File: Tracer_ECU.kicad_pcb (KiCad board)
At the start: 4 copper layers, 82 x 54.8 mm, 148 parts, among them IC1 R5F566TEADFM#30, IC2 MPU-6500, IC3 DRV8300DPWR, IC4 DRV8300DPWR, J1 BAT, J10 ENC2, J11 ENC2_SPI, J12 LCD, J13 SDC, J14 FAN, J15 ENC1_SPI, J2 DBG, J3 TSL1401, J4 MSENS1, J5 MOT1, J6 LIGHIT, J7 MSENS2, J8 MOT2, J9 ENC1, Q1 TJ8S06M3L(T6L1,NQ), Q2 FDS6898A, Q3 FDS6898A, Q4 FDS6898A, Q5 IRLML6344TRPBF, Q6 IRLML6344TRPBF, Q7 FDS6898A, Q8 FDS6898A, Q9 FDS6898A, SW1 SW_SPDT, SW2 SW_Push, SW4 SW_Push, SW5 SW_Push, U1 NJM2732, U2 AZ1117-3.3, Y1 CSTNE20M

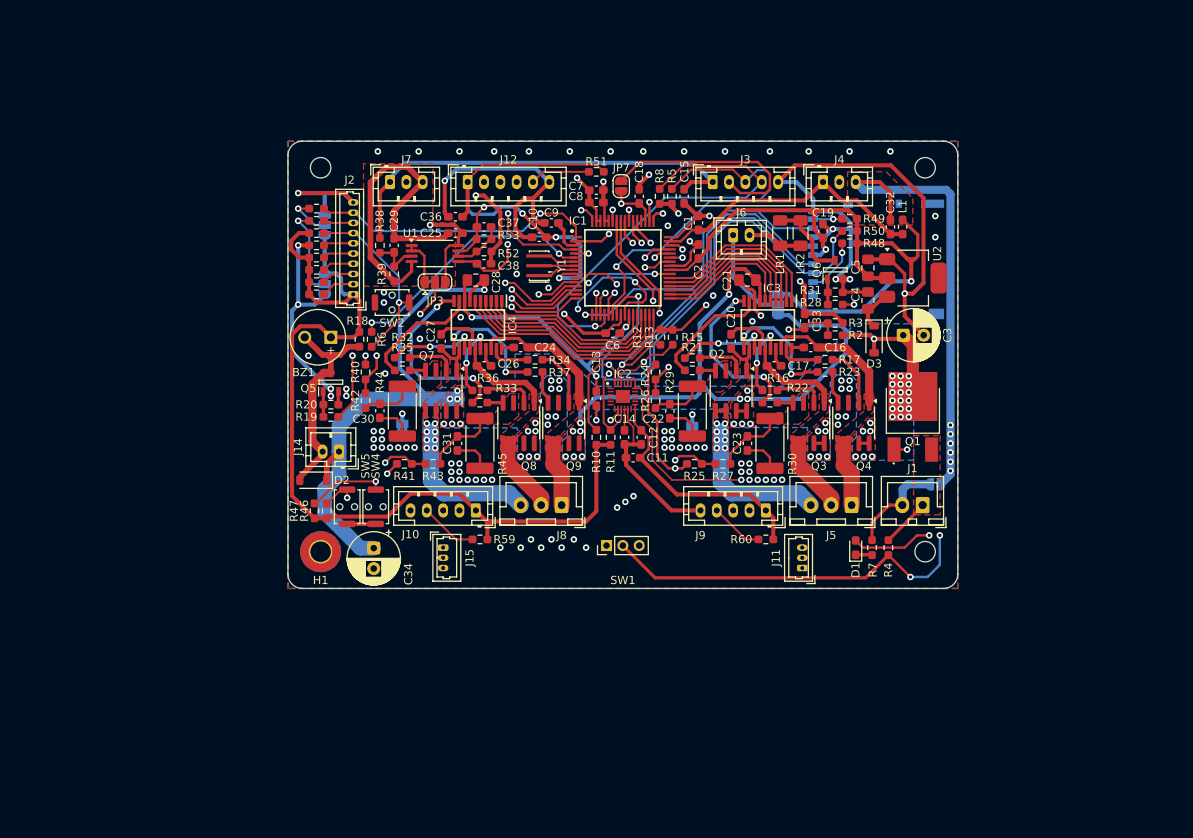
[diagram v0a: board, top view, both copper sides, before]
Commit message: ゲートドライバを変更
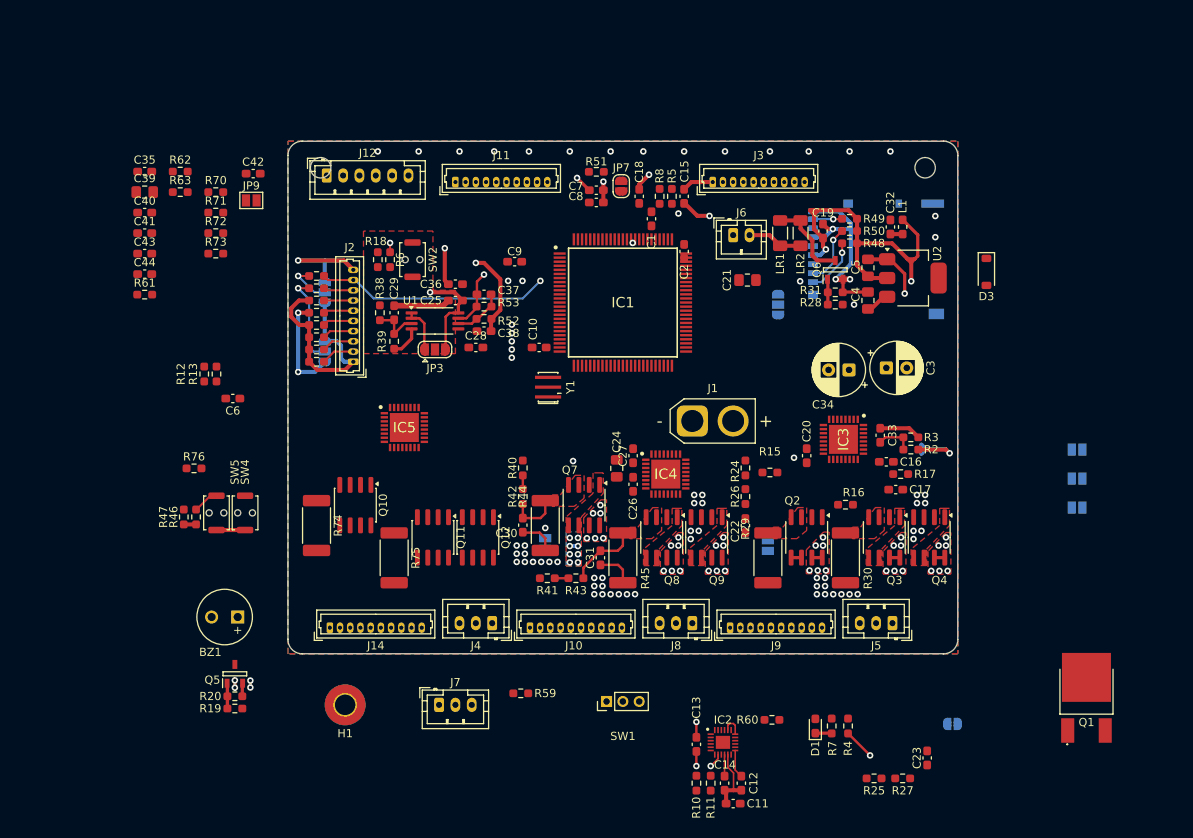
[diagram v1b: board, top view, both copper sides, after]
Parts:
- removed D2: D, Diode_SMD:D_SOD-123
- removed J15: ENC1_SPI, Connector_Molex:Molex_PicoBlade_53047-0310_1x03_P1.25mm_Vertical
- removed R21, R22, R23, R32, R33, R34, R35, R36, R37: 10, Resistor_SMD:R_0603_1608Metric_Pad0.98x0.95mm_HandSolder
- added C35: 0.1u, Capacitor_SMD:C_0603_1608Metric_Pad1.08x0.95mm_HandSolder, F.Cu at (71.0, 68.5)
- added C39: 22u, Capacitor_SMD:C_0805_2012Metric_Pad1.18x1.45mm_HandSolder, F.Cu at (71.0, 71.0)
- added C40: 0.1u, Capacitor_SMD:C_0603_1608Metric_Pad1.08x0.95mm_HandSolder, F.Cu at (71.0, 73.5)
- added C41: 1u, Capacitor_SMD:C_0603_1608Metric_Pad1.08x0.95mm_HandSolder, F.Cu at (71.0, 76.0)
- added C42: 47n, Capacitor_SMD:C_0603_1608Metric_Pad1.08x0.95mm_HandSolder, F.Cu at (84.2, 68.7)
- added C43: 1000p, Capacitor_SMD:C_0603_1608Metric_Pad1.08x0.95mm_HandSolder, F.Cu at (71.0, 78.5)
- added C44: 1000p, Capacitor_SMD:C_0603_1608Metric_Pad1.08x0.95mm_HandSolder, F.Cu at (71.0, 81.0)
- added IC5: DRV8320HRTVR, SamacSys_Parts:QFN50P500X500X80-33N-D, F.Cu at (102.8, 99.8)
- added JP10: JP_or_R, Jumper:SolderJumper-2_P1.3mm_Open_Pad1.0x1.5mm, B.Cu at (185.1, 109.6)
- added JP11: JP_or_R, Jumper:SolderJumper-2_P1.3mm_Open_Pad1.0x1.5mm, B.Cu at (185.1, 106.0)
- added JP12: JP_or_R, Jumper:SolderJumper-2_P1.3mm_Open_Pad1.0x1.5mm, B.Cu at (185.1, 102.5)
- added JP9: JP_or_R, Jumper:SolderJumper-2_P1.3mm_Open_Pad1.0x1.5mm, F.Cu at (84.0, 72.0)
- added Q10: FDS6898A, Package_SO:SOIC-8_3.9x4.9mm_P1.27mm, F.Cu at (96.8, 109.3)
- added Q11: FDS6898A, Package_SO:SOIC-8_3.9x4.9mm_P1.27mm, F.Cu at (106.2, 113.2)
- added Q12: FDS6898A, Package_SO:SOIC-8_3.9x4.9mm_P1.27mm, F.Cu at (111.8, 113.2)
- added R61: 4.7k, Resistor_SMD:R_0603_1608Metric_Pad0.98x0.95mm_HandSolder, F.Cu at (71.0, 83.5)
- added R62: 4.7k, Resistor_SMD:R_0603_1608Metric_Pad0.98x0.95mm_HandSolder, F.Cu at (75.3, 68.5)
- added R63: 4.7k, Resistor_SMD:R_0603_1608Metric_Pad0.98x0.95mm_HandSolder, F.Cu at (75.3, 71.0)
- added R70: 470, Resistor_SMD:R_0603_1608Metric_Pad0.98x0.95mm_HandSolder, F.Cu at (79.7, 71.0)
- added R71: 470, Resistor_SMD:R_0603_1608Metric_Pad0.98x0.95mm_HandSolder, F.Cu at (79.7, 73.5)
- added R72: 470, Resistor_SMD:R_0603_1608Metric_Pad0.98x0.95mm_HandSolder, F.Cu at (79.7, 76.0)
- added R73: 470, Resistor_SMD:R_0603_1608Metric_Pad0.98x0.95mm_HandSolder, F.Cu at (79.7, 78.5)
- added R74: 0.05/1W, Resistor_SMD:R_2512_6332Metric_Pad1.40x3.35mm_HandSolder, F.Cu at (92.0, 111.8)
- added R75: 0.05/1W, Resistor_SMD:R_2512_6332Metric_Pad1.40x3.35mm_HandSolder, F.Cu at (101.5, 115.8)
- added R76: 4.7k, Resistor_SMD:R_0603_1608Metric_Pad0.98x0.95mm_HandSolder, F.Cu at (77.0, 104.8)
- C16: value 2.2u -> 47n
- C17, C27: value 2.2u -> 1u
- C20, C26: value 2.2u -> 0.1u
- C24: value 2.2u -> 22u; footprint Capacitor_SMD:C_0603_1608Metric_Pad1.08x0.95mm_HandSolder -> Capacitor_SMD:C_0805_2012Metric_Pad1.18x1.45mm_HandSolder
- C28: value 22u -> 47n; footprint Capacitor_SMD:C_0805_2012Metric_Pad1.18x1.45mm_HandSolder -> Capacitor_SMD:C_0603_1608Metric_Pad1.08x0.95mm_HandSolder
- IC1: value R5F566TEADFM#30 -> R5F572TFADFP#30; footprint SamacSys_Parts:QFP50P1200X1200X170-64N -> SamacSys_Parts:QFP50P1600X1600X170-100N
- IC3, IC4: value DRV8300DPWR -> DRV8320HRTVR; footprint SamacSys_Parts:SOP65P640X120-20N -> SamacSys_Parts:QFN50P500X500X80-33N-D
- J1: footprint Connector_JST:JST_XH_B2B-XH-A_1x02_P2.50mm_Vertical -> Connector_AMASS:AMASS_XT30U-M_1x02_P5.0mm_Vertical
- J10, J9: footprint Connector_JST:JST_PH_B5B-PH-K_1x05_P2.00mm_Vertical -> Connector_Molex:Molex_PicoBlade_53047-1010_1x10_P1.25mm_Vertical
- J11: value ENC2_SPI -> SENS2; footprint Connector_Molex:Molex_PicoBlade_53047-0310_1x03_P1.25mm_Vertical -> Connector_Molex:Molex_PicoBlade_53047-1010_1x10_P1.25mm_Vertical
- J14: value FAN -> ENC2; footprint Connector_JST:JST_PH_B2B-PH-K_1x02_P2.00mm_Vertical -> Connector_Molex:Molex_PicoBlade_53047-1010_1x10_P1.25mm_Vertical
- J3: value TSL1401 -> SENS1; footprint Connector_JST:JST_PH_B5B-PH-K_1x05_P2.00mm_Vertical -> Connector_Molex:Molex_PicoBlade_53047-1010_1x10_P1.25mm_Vertical
- J4: value MSENS1 -> MOT3
- J5, J8: footprint Connector_JST:JST_XH_B3B-XH-A_1x03_P2.50mm_Vertical -> Connector_JST:JST_PH_B3B-PH-K_1x03_P2.00mm_Vertical
- J7: value MSENS2 -> ESC
- JP2, JP4: value Jumper -> JP_or_R; footprint Jumper:SolderJumper-2_P1.3mm_Bridged2Bar_Pad1.0x1.5mm -> Jumper:SolderJumper-2_P1.3mm_Open_Pad1.0x1.5mm
- R15, R16, R17: value 10 -> 4.7k
- R6: value 220 -> 150
- moved J4 67.5 mm to (113.5, 123.8), turned to 180 degrees
- moved J7 64.3 mm to (107.0, 133.8)
- moved J11 63.5 mm to (109.0, 69.8), turned to 0 degrees
- moved C34 62.1 mm to (157.2, 92.8), turned to 180 degrees
- moved R12 56.0 mm to (78.2, 93.2)
- moved R13 56.0 mm to (79.8, 93.2)
- moved C6 47.2 mm to (81.8, 96.2)
- moved C23 44.3 mm to (166.8, 140.2)
- moved R25 44.3 mm to (160.2, 142.8)
- moved R27 44.3 mm to (163.8, 142.8)
- moved C11 44.1 mm to (143.0, 145.8)
- moved C12 44.1 mm to (144.0, 143.3)
- moved C13 44.1 mm to (138.5, 138.6)
- moved C14 44.1 mm to (141.9, 143.3)
- moved IC2 44.1 mm to (141.8, 138.3)
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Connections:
- C10 pad 2: GND -> Mot.1_SLA
- C11 pad 2: GND -> Mot.1_SLA
- C12 pad 2: GND -> Mot.1_SLA
- C13 pad 2: GND -> Mot.1_SLA
- C14 pad 2: GND -> Mot.1_SLA
- C16 pad 1: Net-(IC3-BSTA) -> Net-(IC3-CPL)
- C16 pad 2: Net-(IC3-SHA) -> Net-(IC3-CPH)
- C17 pad 1: Net-(IC3-BSTB) -> Net-(IC3-VCP)
- C17 pad 2: Net-(IC3-SHB) -> +12V
- C19 pad 2: GND -> Mot.1_SLA
- C2 pad 2: GND -> Mot.1_SLA
- C20 pad 1: Net-(IC3-BSTC) -> Mot.1_SLA
- C20 pad 2: Net-(IC3-SHC) -> +12V
- C21 pad 1: GND -> Mot.1_SLA
- C22 pad 1: Net-(Q2B-S2) -> AN001
- C22 pad 2: GND -> PGAVSS0
- C23 pad 1: Net-(Q3B-S2) -> AN000
- C23 pad 2: GND -> PGAVSS0
- C24 pad 1: Net-(IC4-BSTA) -> Mot.1_SLA
- C24 pad 2: Net-(IC4-SHA) -> +12V
- C26 pad 1: Net-(IC4-BSTB) -> Mot.1_SLA
- C26 pad 2: Net-(IC4-SHB) -> +12V
- C27 pad 1: Net-(IC4-BSTC) -> Net-(IC4-VCP)
- C27 pad 2: Net-(IC4-SHC) -> +12V
- C28 pad 1: GND -> Net-(IC4-CPL)
- C28 pad 2: +12V -> Net-(IC4-CPH)
- C3 pad 2: GND -> Mot.1_SLA
- C30 pad 1: Net-(Q7B-S2) -> AN003
- C30 pad 2: GND -> PGAVSS0
- C31 pad 1: Net-(Q8B-S2) -> AN002
- C31 pad 2: GND -> PGAVSS0
- C33 pad 1: AN002 -> AN103
- C34 pad 2: GND -> Mot.1_SLA
- C36 pad 2: GND -> Mot.1_SLA
- C38 pad 1: Net-(J3-Pin_2) -> Net-(J3-Pin_7)
- C4 pad 2: GND -> Mot.1_SLA
- C5 pad 2: GND -> Mot.1_SLA
- C6 pad 2: GND -> Mot.1_SLA
- C9 pad 2: GND -> Mot.1_SLA
- H1 pad 1: GND -> Mot.1_SLA
- IC1 pad 1: EMLE -> GTIOC3A
- IC1 pad 10: VCC -> RES#
- IC1 pad 11: PE2(CS) -> Net-(IC1-P37/XTAL)
- IC1 pad 12: TRST# -> Mot.1_SLA
- IC1 pad 13: TMS -> Net-(IC1-P36/EXTAL)
- IC1 pad 14: TDI -> VCC
- IC1 pad 15: TCK -> unconnected-(IC1-PE2-Pad15)
- IC1 pad 16: TDO -> SSLA3
- IC1 pad 17: SMISO11 -> SSLA2
- IC1 pad 18: SMOSI11 -> TRST#
- IC1 pad 19: SCK11 -> TMS
- IC1 pad 2: P00/MTIOC9A -> EMLE
- IC1 pad 20: MTIOC0A -> TDI
- IC1 pad 21: PB2(CS) -> TCK
- IC1 pad 22: PB1/MTIOC0C -> TDO
- IC1 pad 23: PB0(CS) -> GTIOC0A
- IC1 pad 24: VCC -> GTIOC0B
- IC1 pad 25: P96/IRQ4 -> GTIOC1A
- IC1 pad 26: GND -> GTIOC1B
- IC1 pad 27: MTIOC6B -> GTIOC2A
- IC1 pad 28: MTIOC7A -> GTIOC2B
- IC1 pad 29: MTIOC7B -> VCC
- IC1 pad 3: Net-(IC1-VCL) -> Mot.1_SLA
- IC1 pad 30: MTIOC6D -> PB4(CS)
- IC1 pad 31: MTIOC7C -> Mot.1_SLA
- IC1 pad 32: MTIOC7D -> RSPCKA
- IC1 pad 33: MTIOC4D -> unconnected-(IC1-PB2-Pad33)
- IC1 pad 34: MTIOC4C -> PB1/MTIOC0C
- IC1 pad 35: MTIOC3D -> MOSIA
- IC1 pad 36: MTIOC4B -> MISOA
- IC1 pad 37: MTIOC4A -> unconnected-(IC1-PA4-Pad37)
- IC1 pad 38: MTIOC3B -> SSLA0
- IC1 pad 39: P70/IRQ5 -> SSLA1
- IC1 pad 4: MD -> MTIOC9A
- IC1 pad 40: VCC -> unconnected-(IC1-PA1-Pad40)
- IC1 pad 41: GND -> unconnected-(IC1-PA0-Pad41)
- IC1 pad 42: MTCLKD -> VCC
- IC1 pad 43: MTCLKA -> unconnected-(IC1-P96-Pad43)
- IC1 pad 44: MTCLKB -> Mot.1_SLA
- IC1 pad 45: P65/IRQ9/DA1 -> MTIOC6B
- IC1 pad 46: P64/IRQ8/DA0 -> MTIOC7A
- IC1 pad 47: VDDA -> MTIOC7B
- IC1 pad 48: GNDA -> MTIOC6D
- IC1 pad 49: AN202/IRQ2 -> MTIOC7C
- IC1 pad 5: MTIOC9C -> Net-(IC1-VCL)
- IC1 pad 50: AN201/IRQ1 -> MTIOC7D
- IC1 pad 51: AN200 -> MTIOC4D
- IC1 pad 52: unconnected-(IC1-P46-Pad52) -> MTIOC4C
- IC1 pad 53: AN101 -> MTIOC3D
- IC1 pad 54: AN100 -> MTIOC4B
- IC1 pad 55: PGAVSS1 -> MTIOC4A
- IC1 pad 56: AN002 -> MTIOC3B
- IC1 pad 57: AN001 -> IRQ5
- IC1 pad 58: AN000 -> MTCLKA
- IC1 pad 59: PGAVSS0 -> MTCLKB
- IC1 pad 6: RES# -> MD
- IC1 pad 60: VDDA -> VCC
- IC1 pad 61: VDDA -> MTIOC0A
- IC1 pad 62: GNDA -> Mot.1_SLA
- IC1 pad 63: GNDA -> unconnected-(IC1-P30-Pad63)
- IC1 pad 64: MTCLKC -> unconnected-(IC1-P27-Pad64)
- IC1 pad 7: Net-(IC1-P37/XTAL) -> IRQ4
- IC1 pad 8: GND -> MTCLKC
- IC1 pad 9: Net-(IC1-P36/EXTAL) -> MTCLKD
- IC2 pad 11: GND -> Mot.1_SLA
- IC2 pad 18: GND -> Mot.1_SLA
- IC2 pad 20: GND -> Mot.1_SLA
- IC2 pad 22: PE2(CS) -> SSLA0
- IC2 pad 23: SCK11 -> RSPCKA
- IC2 pad 24: SMOSI11 -> MOSIA
- IC2 pad 9: SMISO11 -> MISOA
- IC3 pad 1: MTIOC3B -> Net-(IC3-CPH)
- IC3 pad 10: Mot.1_VL -> Mot.1_GLB
- IC3 pad 11: Mot.1_UL -> Mot.1_SHB
- IC3 pad 12: Net-(IC3-SHC) -> Mot.1_GHB
- IC3 pad 13: Mot.1_WH -> Mot.1_GHC
- IC3 pad 14: Net-(IC3-BSTC) -> Mot.1_SHC
- IC3 pad 15: Net-(IC3-SHB) -> Mot.1_GLC
- IC3 pad 16: Mot.1_VH -> Mot.1_SLC
- IC3 pad 17: Net-(IC3-BSTB) -> Mot.1_nFAULT
- IC3 pad 18: Net-(IC3-SHA) -> Net-(IC3-AGND)
- IC3 pad 19: Mot.1_UH -> Net-(IC3-DVDD)
- IC3 pad 2: MTIOC4A -> Net-(IC3-VCP)
- IC3 pad 20: Net-(IC3-BSTA) -> Net-(IC3-DVDD)
- IC3 pad 3: MTIOC4B -> +12V
- IC3 pad 4: MTIOC3D -> +12V
- IC3 pad 5: MTIOC4C -> Mot.1_GHA
- IC3 pad 6: MTIOC4D -> Mot.1_SHA
- IC3 pad 7: +12V -> Mot.1_GLA
- IC3 pad 8: GND -> Mot.1_SLA
- IC3 pad 9: Mot.1_WL -> Mot.1_SLB
- IC4 pad 1: MTIOC6B -> Net-(IC4-CPH)
- IC4 pad 10: Mot.2_VL -> Mot.2_GLB
- IC4 pad 11: Mot.2_UL -> Mot.2_SHB
- IC4 pad 12: Net-(IC4-SHC) -> Mot.2_GHB
- IC4 pad 13: Mot.2_WH -> Mot.2_GHC
- IC4 pad 14: Net-(IC4-BSTC) -> Mot.2_SHC
- IC4 pad 15: Net-(IC4-SHB) -> Mot.2_GLC
- IC4 pad 16: Mot.2_VH -> Mot.2_SLC
- IC4 pad 17: Net-(IC4-BSTB) -> Mot.2_nFAULT
- IC4 pad 18: Net-(IC4-SHA) -> Net-(IC4-AGND)
- IC4 pad 19: Mot.2_UH -> Net-(IC4-DVDD)
- IC4 pad 2: MTIOC7A -> Net-(IC4-VCP)
- IC4 pad 20: Net-(IC4-BSTA) -> Net-(IC4-DVDD)
- IC4 pad 3: MTIOC7B -> +12V
- IC4 pad 4: MTIOC6D -> +12V
- IC4 pad 5: MTIOC7C -> Mot.2_GHA
- IC4 pad 6: MTIOC7D -> Mot.2_SHA
- IC4 pad 7: +12V -> Mot.2_GLA
- IC4 pad 8: GND -> Mot.1_SLA
- IC4 pad 9: Mot.2_WL -> Mot.2_SLB
- J1 pad 1: Net-(J1-Pin_1) -> Mot.1_SLA
- J1 pad 2: GND -> Net-(J1-Pin_2)
- J10 pad 2: MTCLKC -> MOSIA
- J10 pad 3: MTCLKD -> MISOA
- J10 pad 4: P65/IRQ9/DA1 -> RSPCKA
- J10 pad 5: GND -> SSLA2
- J11 pad 1: SMISO11 -> AN200
- J11 pad 2: SMOSI11 -> AN201
- J11 pad 3: SCK11 -> AN202
- J12 pad 2: SMISO11 -> MOSIA
- J12 pad 3: SMOSI11 -> MISOA
- J12 pad 4: SCK11 -> RSPCKA
- J12 pad 5: PB2(CS) -> SSLA3
- J12 pad 6: GND -> Mot.1_SLA
- J13 pad 2: PB0(CS) -> PB4(CS)
- J13 pad 3: SMOSI11 -> SMOSI12
- J13 pad 5: SCK11 -> SCK12
- J13 pad 6: GND -> Mot.1_SLA
- J13 pad 7: SMISO11 -> SMISO12
- J13 pad 9: GND -> Mot.1_SLA
- J14 pad 1: +12V -> VCC
- J14 pad 2: Net-(BZ1--) -> MOSIA
- J2 pad 10: GND -> Mot.1_SLA
- J3 pad 2: Net-(J3-Pin_2) -> VDDA
- J3 pad 3: PB1/MTIOC0C -> AN216/IRQ7
- J3 pad 4: MTIOC0A -> AN217/IRQ6
- J3 pad 5: GND -> GNDA
- J4 pad 1: VDDA -> Mot.3_SHA
- J4 pad 2: AN202/IRQ2 -> Mot.3_SHB
- J4 pad 3: GNDA -> Mot.3_SHC
- J5 pad 1: Net-(IC3-SHA) -> Mot.1_SHA
- J5 pad 2: Net-(IC3-SHB) -> Mot.1_SHB
- J5 pad 3: Net-(IC3-SHC) -> Mot.1_SHC
- J7 pad 1: VDDA -> Mot.1_SLA
- J7 pad 2: AN201/IRQ1 -> MTIOC9A
- J7 pad 3: GNDA -> +12V
- J8 pad 1: Net-(IC4-SHA) -> Mot.2_SHA
- J8 pad 2: Net-(IC4-SHB) -> Mot.2_SHB
- J8 pad 3: Net-(IC4-SHC) -> Mot.2_SHC
- J9 pad 2: MTCLKA -> MOSIA
- J9 pad 3: MTCLKB -> MISOA
- J9 pad 4: P64/IRQ8/DA0 -> RSPCKA
- J9 pad 5: GND -> SSLA1
- JP1 pad 1: GND -> Mot.1_SLA
- JP2 pad 1: PGAVSS1 -> PGAVSS0
- JP2 pad 2: GND -> Mot.1_SLA
- JP4 pad 2: GND -> Mot.1_SLA
- JP5 pad 1: GND -> Mot.1_SLA
- JP6 pad 1: GND -> Mot.1_SLA
- JP7 pad 1: Net-(J3-Pin_2) -> Net-(J3-Pin_7)
- Q1 pad 3: Net-(J1-Pin_1) -> Net-(J1-Pin_2)
- Q2 pad 1: Net-(IC3-SHC) -> Mot.1_SHC
- Q2 pad 2: Net-(Q2A-G1) -> Mot.1_GHC
- Q2 pad 3: Net-(Q2B-S2) -> Mot.1_SLC
- Q2 pad 4: Net-(Q2B-G2) -> Mot.1_GLC
- Q2 pad 5: Net-(IC3-SHC) -> Mot.1_SHC
- Q2 pad 6: Net-(IC3-SHC) -> Mot.1_SHC
- Q3 pad 1: Net-(IC3-SHB) -> Mot.1_SHB
- Q3 pad 2: Net-(Q3A-G1) -> Mot.1_GHB
- Q3 pad 3: Net-(Q3B-S2) -> Mot.1_SLB
- Q3 pad 4: Net-(Q3B-G2) -> Mot.1_GLB
- Q3 pad 5: Net-(IC3-SHB) -> Mot.1_SHB
- Q3 pad 6: Net-(IC3-SHB) -> Mot.1_SHB
- Q4 pad 1: Net-(IC3-SHA) -> Mot.1_SHA
- Q4 pad 2: Net-(Q4A-G1) -> Mot.1_GHA
- Q4 pad 3: GND -> Mot.1_SLA
- Q4 pad 4: Net-(Q4B-G2) -> Mot.1_GLA
- Q4 pad 5: Net-(IC3-SHA) -> Mot.1_SHA
- Q4 pad 6: Net-(IC3-SHA) -> Mot.1_SHA
- Q5 pad 2: GND -> Mot.1_SLA
- Q6 pad 2: GND -> Mot.1_SLA
- Q7 pad 1: Net-(IC4-SHC) -> Mot.2_SHC
- Q7 pad 2: Net-(Q7A-G1) -> Mot.2_GHC
- Q7 pad 3: Net-(Q7B-S2) -> Mot.2_SLC
- Q7 pad 4: Net-(Q7B-G2) -> Mot.2_GLC
- Q7 pad 5: Net-(IC4-SHC) -> Mot.2_SHC
- Q7 pad 6: Net-(IC4-SHC) -> Mot.2_SHC
- Q8 pad 1: Net-(IC4-SHB) -> Mot.2_SHB
- Q8 pad 2: Net-(Q8A-G1) -> Mot.2_GHB
- Q8 pad 3: Net-(Q8B-S2) -> Mot.2_SLB
- Q8 pad 4: Net-(Q8B-G2) -> Mot.2_GLB
- Q8 pad 5: Net-(IC4-SHB) -> Mot.2_SHB
- Q8 pad 6: Net-(IC4-SHB) -> Mot.2_SHB
- Q9 pad 1: Net-(IC4-SHA) -> Mot.2_SHA
- Q9 pad 2: Net-(Q9A-G1) -> Mot.2_GHA
- Q9 pad 3: GND -> Mot.1_SLA
- Q9 pad 4: Net-(Q9B-G2) -> Mot.2_GLA
- Q9 pad 5: Net-(IC4-SHA) -> Mot.2_SHA
- Q9 pad 6: Net-(IC4-SHA) -> Mot.2_SHA
- R10 pad 1: VCC -> MOSIA
- R10 pad 2: SMOSI11 -> VCC
- R11 pad 1: VCC -> MISOA
- R11 pad 2: SMISO11 -> VCC
- R12 pad 1: VCC -> RSPCKA
- R12 pad 2: SCK11 -> VCC
- R13 pad 2: PE2(CS) -> SSLA0
- R15 pad 1: Net-(Q2A-G1) -> VCC
- R15 pad 2: Mot.1_WH -> Mot.1_nFAULT
- R16 pad 1: Net-(Q3A-G1) -> VCC
- R16 pad 2: Mot.1_VH -> Mot.2_nFAULT
- R17 pad 1: Net-(Q4A-G1) -> VCC
- R17 pad 2: Mot.1_UH -> Mot.3_nFAULT
- R19 pad 2: MTIOC9C -> GTIOC3A
- R2 pad 2: AN002 -> AN103
- R20 pad 1: GND -> Mot.1_SLA
- R24 pad 2: AN000 -> AN001
- R25 pad 2: AN001 -> AN000
- R26 pad 1: Net-(Q2B-S2) -> Mot.1_SLC
- R26 pad 2: AN000 -> AN001
- R27 pad 1: Net-(Q3B-S2) -> Mot.1_SLB
- R27 pad 2: AN001 -> AN000
- R28 pad 2: P00/MTIOC9A -> unconnected-(R28-Pad2)
- R29 pad 1: Net-(Q2B-S2) -> Mot.1_SLC
- R29 pad 2: GND -> Mot.1_SLA
- R3 pad 1: AN002 -> AN103
- R30 pad 1: Net-(Q3B-S2) -> Mot.1_SLB
- R30 pad 2: GND -> Mot.1_SLA
- R31 pad 1: GND -> Mot.1_SLA
- R4 pad 1: Net-(J1-Pin_1) -> Net-(J1-Pin_2)
- R40 pad 2: AN100 -> AN003
- R41 pad 2: AN101 -> AN002
- R42 pad 1: Net-(Q7B-S2) -> Mot.2_SLC
- R42 pad 2: AN100 -> AN003
- R43 pad 1: Net-(Q8B-S2) -> Mot.2_SLB
- R43 pad 2: AN101 -> AN002
- R44 pad 1: Net-(Q7B-S2) -> Mot.2_SLC
- R44 pad 2: GND -> Mot.1_SLA
- R45 pad 1: Net-(Q8B-S2) -> Mot.2_SLB
- R45 pad 2: GND -> Mot.1_SLA
- R46 pad 2: P96/IRQ4 -> unconnected-(R46-Pad2)
- R47 pad 2: P70/IRQ5 -> unconnected-(R47-Pad2)
- R5 pad 2: GND -> Mot.1_SLA
- R50 pad 2: PB0(CS) -> PB4(CS)
- R51 pad 2: PB2(CS) -> SSLA3
- R56 pad 2: GND -> Mot.1_SLA
- R59 pad 2: P65/IRQ9/DA1 -> SSLA2
- R60 pad 2: P64/IRQ8/DA0 -> SSLA1
- R7 pad 2: GND -> Mot.1_SLA
- R8 pad 2: GND -> Mot.1_SLA
- SW1 pad 3: GND -> Mot.1_SLA
- SW2 pad 1: GND -> Mot.1_SLA
- SW4 pad 1: P96/IRQ4 -> unconnected-(R46-Pad2)
- SW4 pad 2: GND -> Mot.1_SLA
- SW5 pad 1: P70/IRQ5 -> unconnected-(R47-Pad2)
- SW5 pad 2: GND -> Mot.1_SLA
- U1 pad 5: Net-(J3-Pin_2) -> Net-(J3-Pin_7)
- U2 pad 1: GND -> Mot.1_SLA
- Y1 pad 2: GND -> Mot.1_SLA
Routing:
- net VCC: track 544.9 -> 79.8 mm, vias 9 -> 5
- net GND: track 425.2 -> 0.00 mm, vias 104 -> 0
- net +12V: track 196.0 -> 13.6 mm, vias 58 -> 37
- net GNDA: track 226.9 -> 44.7 mm, vias 11 -> 5
- net SMOSI11: track 177.6 -> 0.00 mm, vias 3 -> 0
- net SMISO11: track 170.3 -> 0.00 mm, vias 3 -> 0
- net SCK11: track 165.9 -> 0.00 mm, vias 3 -> 0
- net VDDA: track 141.7 -> 33.2 mm
- net Mot.1_SLA: track 0.00 -> 96.4 mm, vias 0 -> 74
- net Net-(JP3-C): track 85.3 -> 0.00 mm, vias 4 -> 0
- net P65/IRQ9/DA1: track 75.4 -> 0.00 mm, vias 1 -> 0
- net MTCLKC: track 68.7 -> 0.00 mm, vias 1 -> 0
- net Net-(J3-Pin_2): track 67.3 -> 0.00 mm, vias 1 -> 0
- net PB0(CS): track 64.7 -> 0.00 mm, vias 2 -> 0
- net MTCLKD: track 64.3 -> 0.00 mm, vias 1 -> 0
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- added copper zone on F.Cu, net Mot.1_SHA
- added copper zone on F.Cu, net Mot.1_SHB
- added copper zone on B.Cu, net Mot.1_SLA
- added copper zone on F.Cu, net Mot.1_SLA
- added copper zone on In1.Cu, net Mot.1_SLA
- added copper zone on F.Cu, net Mot.1_SLB
- added copper zone on F.Cu, net Mot.1_SLC
- added copper zone on F.Cu, net Mot.2_SHA
- added copper zone on F.Cu, net Mot.2_SHB
- added copper zone on B.Cu, net Mot.2_SHC
- added copper zone on F.Cu, net Mot.2_SHC
- added copper zone on F.Cu, net Mot.2_SLB
- added copper zone on F.Cu, net Mot.2_SLC
- removed copper zone on B.Cu, net +12V
- removed copper zone on B.Cu, net GND
- removed copper zone on F.Cu, net GND
- removed copper zone on In1.Cu, net GND
- removed copper zone on F.Cu, net Net-(IC3-SHA)
- removed copper zone on F.Cu, net Net-(IC3-SHB)
- removed copper zone on B.Cu, net Net-(IC3-SHC)
- removed copper zone on F.Cu, net Net-(IC3-SHC)
- removed copper zone on F.Cu, net Net-(IC4-SHA)
- removed copper zone on F.Cu, net Net-(IC4-SHB)
- removed copper zone on B.Cu, net Net-(IC4-SHC)
- removed copper zone on F.Cu, net Net-(IC4-SHC)
- removed copper zone on F.Cu, net Net-(J1-Pin_1)
- removed copper zone on F.Cu, net Net-(Q2B-S2)
- removed copper zone on F.Cu, net Net-(Q3B-S2)
- removed copper zone on F.Cu, net Net-(Q7B-S2)
- removed copper zone on F.Cu, net Net-(Q8B-S2)
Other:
- board size 82 x 54.8 mm -> 82 x 62.8 mm

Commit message: 配線途中をコミット
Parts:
- Q1: moved to B.Cu
- moved C23 79.5 mm to (126.4, 71.8), turned to 0 degrees
- moved R27 77.6 mm to (126.4, 74.8)
- moved R25 77.3 mm to (126.4, 73.2), turned to 180 degrees
- moved C18 75.1 mm to (110.2, 143.5), turned to 0 degrees
- moved JP2 65.1 mm to (185.0, 117.0), turned to 0 degrees
- moved C3 64.6 mm to (118.2, 140.2), turned to 90 degrees
- moved C11 61.2 mm to (147.2, 84.8)
- moved C12 61.2 mm to (148.2, 82.2)
- moved C13 61.2 mm to (142.8, 77.5)
- moved C14 61.2 mm to (146.2, 82.2)
- moved IC2 61.2 mm to (146.0, 77.2)
- moved R10 61.2 mm to (142.8, 82.2)
- moved R11 61.2 mm to (144.5, 82.2)
- moved C34 57.8 mm to (131.2, 144.4), turned to 90 degrees
- moved SW1 55.0 mm to (182.5, 132.8), turned to 0 degrees
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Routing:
- net +12V: track 13.6 -> 65.0 mm, vias 37 -> 55
- net VDDA: track 33.2 -> 80.1 mm, vias 2 -> 3
- net GNDA: track 44.7 -> 16.4 mm, vias 5 -> 2
- net Mot.1_SLA: track 96.4 -> 68.4 mm, vias 74 -> 86
- net Mot.3_SHC: track 0.00 -> 22.3 mm, vias 0 -> 1
- net Mot.1_SHC: track 1.27 -> 23.5 mm, vias 0 -> 1
- net Mot.2_SHC: track 1.00 -> 22.3 mm, vias 8 -> 1
- net Mot.3_SHB: track 0.00 -> 17.6 mm, vias 0 -> 1
- net Mot.2_SHB: track 0.00 -> 17.6 mm, vias 0 -> 1
- net Mot.1_SHB: track 0.00 -> 17.5 mm, vias 0 -> 1
- net Mot.1_GHC: track 0.00 -> 17.3 mm
- net Mot.3_GHC: track 0.00 -> 17.3 mm
- net Mot.2_GHC: track 0.00 -> 17.2 mm
- net Mot.1_SLC: track 0.00 -> 16.6 mm, vias 0 -> 3
- net Mot.3_SLC: track 0.00 -> 16.4 mm, vias 0 -> 3
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- added copper zone on B.Cu, net +12V
- added copper zone on F.Cu, net Mot.1_SHC
- added copper zone on F.Cu, net Mot.3_SHA
- added copper zone on F.Cu, net Mot.3_SHB
- added copper zone on F.Cu, net Mot.3_SHC
- added copper zone on F.Cu, net Mot.3_SLB
- added copper zone on F.Cu, net Mot.3_SLC
- removed copper zone on B.Cu, net Mot.2_SHC
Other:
- board size 82 x 62.8 mm -> 82 x 56 mm

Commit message: SPI系配線完了
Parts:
- removed BZ1: Buzzer, Buzzer_Beeper:MagneticBuzzer_Kingstate_KCG0601
- removed C36: 0.1u, Capacitor_SMD:C_0603_1608Metric_Pad1.08x0.95mm_HandSolder
- removed J12: LCD, Connector_JST:JST_PH_B6B-PH-K_1x06_P2.00mm_Vertical
- removed Q5: IRLML6344TRPBF, SamacSys_Parts:SOT95P260X110-3N
- removed R17, R51: 4.7k, Resistor_SMD:R_0603_1608Metric_Pad0.98x0.95mm_HandSolder
- removed R18: 1k, Resistor_SMD:R_0603_1608Metric_Pad0.98x0.95mm_HandSolder
- removed R19: 470, Resistor_SMD:R_0603_1608Metric_Pad0.98x0.95mm_HandSolder
- removed R20: 100k, Resistor_SMD:R_0603_1608Metric_Pad0.98x0.95mm_HandSolder
- J14: value ENC2 -> ENC3
- JP8: moved to F.Cu
- R52: value 10k -> X1
- R53: value 10k -> X2
- moved R15 80.2 mm to (113.5, 90.2)
- moved R16 76.0 mm to (101.2, 80.0), turned to -90 degrees
- moved C18 56.0 mm to (120.8, 88.5), turned to -90 degrees
- moved C43 54.0 mm to (123.8, 89.8), turned to 90 degrees
- moved C44 53.0 mm to (123.8, 86.2), turned to -90 degrees
- moved R70 50.0 mm to (126.2, 89.0), turned to 180 degrees
- moved R72 48.8 mm to (126.2, 90.5), turned to 180 degrees
- moved C34 48.3 mm to (115.8, 98.7)
- moved R71 48.1 mm to (126.2, 85.5), turned to 180 degrees
- moved R10 48.0 mm to (190.8, 81.0), turned to -90 degrees
- moved R11 47.8 mm to (192.2, 81.0), turned to -90 degrees
- moved R73 47.4 mm to (126.2, 87.0), turned to 180 degrees
- moved C3 47.0 mm to (140.2, 98.7)
- moved Q6 44.5 mm to (153.5, 86.9)
- moved J6 44.2 mm to (148.2, 75.5), turned to 180 degrees
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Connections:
- IC1 pad 100: unconnected-(IC1-P10-Pad100) -> IRQ0
- IC1 pad 33: unconnected-(IC1-PB2-Pad33) -> PB2(GD_EN)
- IC1 pad 43: unconnected-(IC1-P96-Pad43) -> P96(LIGHIT)
- IC1 pad 64: unconnected-(IC1-P27-Pad64) -> IRQ15
- IC1 pad 99: unconnected-(IC1-P11-Pad99) -> GTIOC3B
- IC2 pad 25: unconnected-(IC2-T_PAD-Pad25) -> Mot.1_SLA
- IC3 pad 17: Mot.1_nFAULT -> IRQ15
- IC3 pad 22: unconnected-(IC3-ENABLE-Pad22) -> PB2(GD_EN)
- IC4 pad 17: Mot.2_nFAULT -> IRQ15
- IC4 pad 22: unconnected-(IC4-ENABLE-Pad22) -> PB2(GD_EN)
- IC5 pad 17: Mot.3_nFAULT -> IRQ15
- IC5 pad 22: unconnected-(IC5-ENABLE-Pad22) -> PB2(GD_EN)
- J11 pad 1: AN200 -> AN211/DA1
- J11 pad 10: AN211/DA1 -> AN200
- J11 pad 2: AN201 -> AN210/DA0
- J11 pad 3: AN202 -> AN209
- J11 pad 4: AN203 -> AN208
- J11 pad 5: AN206 -> AN207
- J11 pad 6: AN207 -> AN206
- J11 pad 7: AN208 -> AN203
- J11 pad 8: AN209 -> AN202
- J11 pad 9: AN210/DA0 -> AN201
- J14 pad 5: SSLA2 -> SSLA3
- J14 pad 6: MTCLKC -> GTIOC3A
- J14 pad 7: MTCLKD -> GTIOC3B
- J14 pad 8: IRQ4 -> IRQ0
- R15 pad 2: Mot.1_nFAULT -> IRQ15
- R16 pad 1: VCC -> PB2(GD_EN)
- R16 pad 2: Mot.2_nFAULT -> Mot.1_SLA
- R28 pad 2: unconnected-(R28-Pad2) -> P96(LIGHIT)
- R76 pad 2: SSLA2 -> SSLA3
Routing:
- net RSPCKA: track 0.00 -> 189.8 mm, vias 0 -> 4
- net MOSIA: track 0.00 -> 180.8 mm, vias 0 -> 2
- net MISOA: track 0.00 -> 148.0 mm, vias 0 -> 2
- net MTIOC0A: track 0.00 -> 78.3 mm, vias 0 -> 1
- net MTIOC4D: track 0.00 -> 62.3 mm, vias 0 -> 2
- net AN216/IRQ7: track 0.00 -> 61.0 mm, vias 0 -> 2
- net PB1/MTIOC0C: track 0.00 -> 56.4 mm, vias 0 -> 1
- net P96(LIGHIT): track 0.00 -> 56.3 mm, vias 0 -> 2
- net MTIOC3D: track 0.00 -> 55.3 mm, vias 0 -> 2
- net Mot.1_SLC: track 16.6 -> 71.6 mm, vias 3 -> 4
- net MTIOC4C: track 0.00 -> 54.3 mm, vias 0 -> 2
- net AN217/IRQ6: track 0.00 -> 54.3 mm, vias 0 -> 1
- net MTIOC3B: track 0.00 -> 53.8 mm, vias 0 -> 2
- net MTIOC4B: track 0.00 -> 52.7 mm, vias 0 -> 2
- net MTIOC4A: track 0.00 -> 50.7 mm, vias 0 -> 2
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- removed copper zone on F.Cu, net GNDA
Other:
- board size 82 x 56 mm -> 82 x 60 mm

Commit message: ・未配線数０まで完了
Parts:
- removed D1: LED, LED_SMD:LED_0603_1608Metric_Pad1.05x0.95mm_HandSolder
- removed J7: ESC, Connector_JST:JST_PH_B3B-PH-K_1x03_P2.00mm_Vertical
- removed JP10, JP11, JP12, JP2, JP4, JP9: JP_or_R, Jumper:SolderJumper-2_P1.3mm_Open_Pad1.0x1.5mm
- added LED1: LED, LED_SMD:LED_0603_1608Metric_Pad1.05x0.95mm_HandSolder, F.Cu at (164.0, 109.0)
- added R17: 4.7k, Resistor_SMD:R_0603_1608Metric_Pad0.98x0.95mm_HandSolder, F.Cu at (146.8, 73.2)
- JP5: moved to F.Cu
- moved R61 82.6 mm to (153.2, 76.2)
- moved R62 78.1 mm to (153.2, 73.2)
- moved R63 78.0 mm to (153.2, 74.8)
- moved H1 72.4 mm to (166.5, 119.8)
- moved R12 68.5 mm to (143.2, 115.0), turned to 90 degrees
- moved R13 64.7 mm to (142.0, 75.8), turned to 0 degrees
- moved R10 60.9 mm to (140.2, 115.0), turned to 90 degrees
- moved R11 60.9 mm to (141.8, 115.0), turned to 90 degrees
- moved JP5 59.4 mm to (165.2, 76.9), turned to 90 degrees
- moved C33 53.9 mm to (121.2, 87.8), turned to -90 degrees
- moved R3 43.6 mm to (135.5, 115.8), turned to 180 degrees
- moved R2 42.8 mm to (135.5, 114.2), turned to 0 degrees
- moved R76 38.6 mm to (112.2, 120.5), turned to 90 degrees
- moved R4 34.3 mm to (162.8, 103.0), turned to 180 degrees
- moved R7 28.8 mm to (162.2, 109.0)
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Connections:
- C22 pad 2: PGAVSS0 -> Mot.1_SLA
- C23 pad 2: PGAVSS0 -> Mot.1_SLA
- C30 pad 2: PGAVSS0 -> Mot.1_SLA
- C31 pad 2: PGAVSS0 -> Mot.1_SLA
- C43 pad 2: PGAVSS1 -> Mot.1_SLA
- C44 pad 2: PGAVSS1 -> Mot.1_SLA
- IC1 pad 63: unconnected-(IC1-P30-Pad63) -> P30
- IC1 pad 65: unconnected-(IC1-P24-Pad65) -> P24
- IC1 pad 86: PGAVSS1 -> Mot.1_SLA
- IC1 pad 91: PGAVSS0 -> Mot.1_SLA
- IC1 pad 97: unconnected-(IC1-P81-Pad97) -> TXD6
- IC1 pad 98: unconnected-(IC1-P80-Pad98) -> RXD6
- J3 pad 5: GNDA -> MTIOC9A
- R46 pad 2: unconnected-(R46-Pad2) -> P24
- R47 pad 2: unconnected-(R47-Pad2) -> P30
- SW4 pad 1: unconnected-(R46-Pad2) -> P24
- SW5 pad 1: unconnected-(R47-Pad2) -> P30
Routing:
- net VCC: track 101.8 -> 419.3 mm, vias 5 -> 9
- net GNDA: track 17.8 -> 158.9 mm, vias 0 -> 23
- net IRQ4: track 0.00 -> 123.1 mm, vias 0 -> 2
- net MTCLKC: track 0.00 -> 117.2 mm, vias 0 -> 2
- net MTCLKD: track 0.00 -> 116.3 mm, vias 0 -> 2
- net GTIOC3B: track 0.00 -> 101.0 mm, vias 0 -> 3
- net IRQ0: track 0.00 -> 99.7 mm, vias 0 -> 2
- net GTIOC3A: track 0.00 -> 98.2 mm, vias 0 -> 3
- net Mot.1_SLA: track 59.8 -> 156.8 mm, vias 65 -> 163
- net IRQ15: track 2.46 -> 93.6 mm, vias 0 -> 4
- net SSLA3: track 0.00 -> 90.4 mm, vias 0 -> 2
- net SSLA2: track 0.00 -> 87.6 mm, vias 0 -> 2
- net SSLA1: track 0.00 -> 84.6 mm, vias 0 -> 2
- net PB2(GD_EN): track 2.46 -> 86.3 mm, vias 0 -> 6
- net IRQ5: track 0.00 -> 76.4 mm, vias 0 -> 2
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- added copper zone on F.Cu, net GNDA
- added copper zone on B.Cu, net Net-(J1-Pin_2)
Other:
- outline, holes or cut-outs redrawn
